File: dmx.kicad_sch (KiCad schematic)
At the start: 41 parts, among them J101 SJ2-25504B-SMT-TR, J102 CORTEX-DEBUG, J103 JAE_DX07S016JA1R1500, SW101 SW_Push, SW102 SW_Push, U101 LTC2851xDD, U102 ATSAMD51G, U103 AP2112K-3.3, Y101 32.768kHz

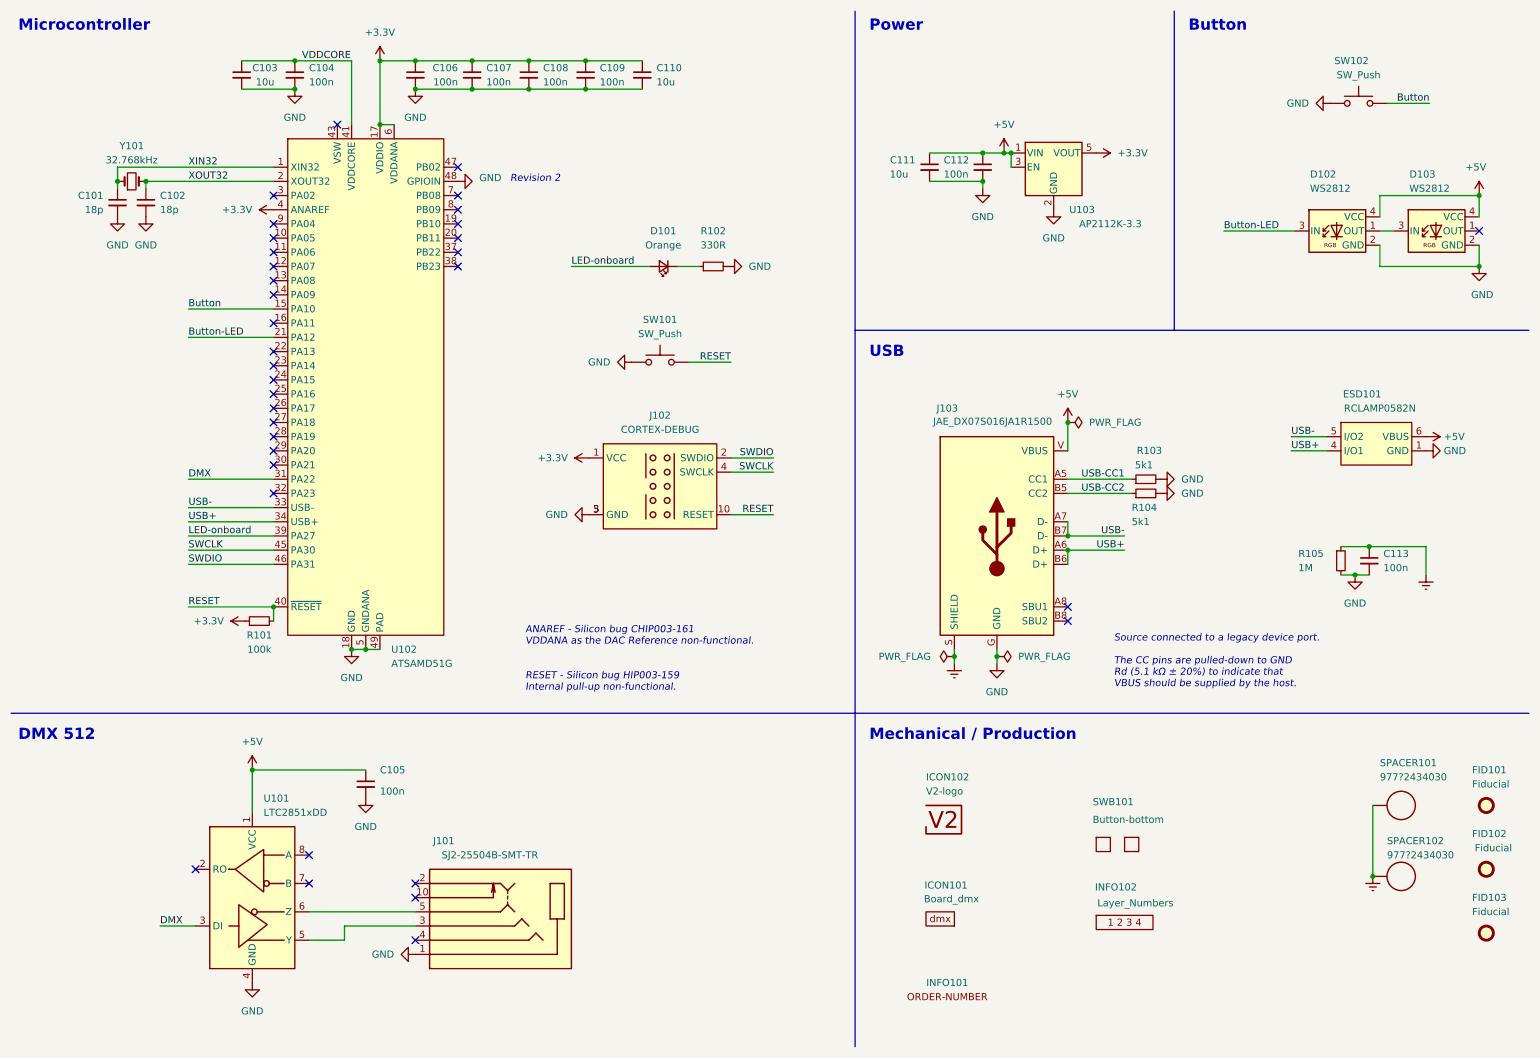
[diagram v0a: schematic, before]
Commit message: Update to KiCad 7.0
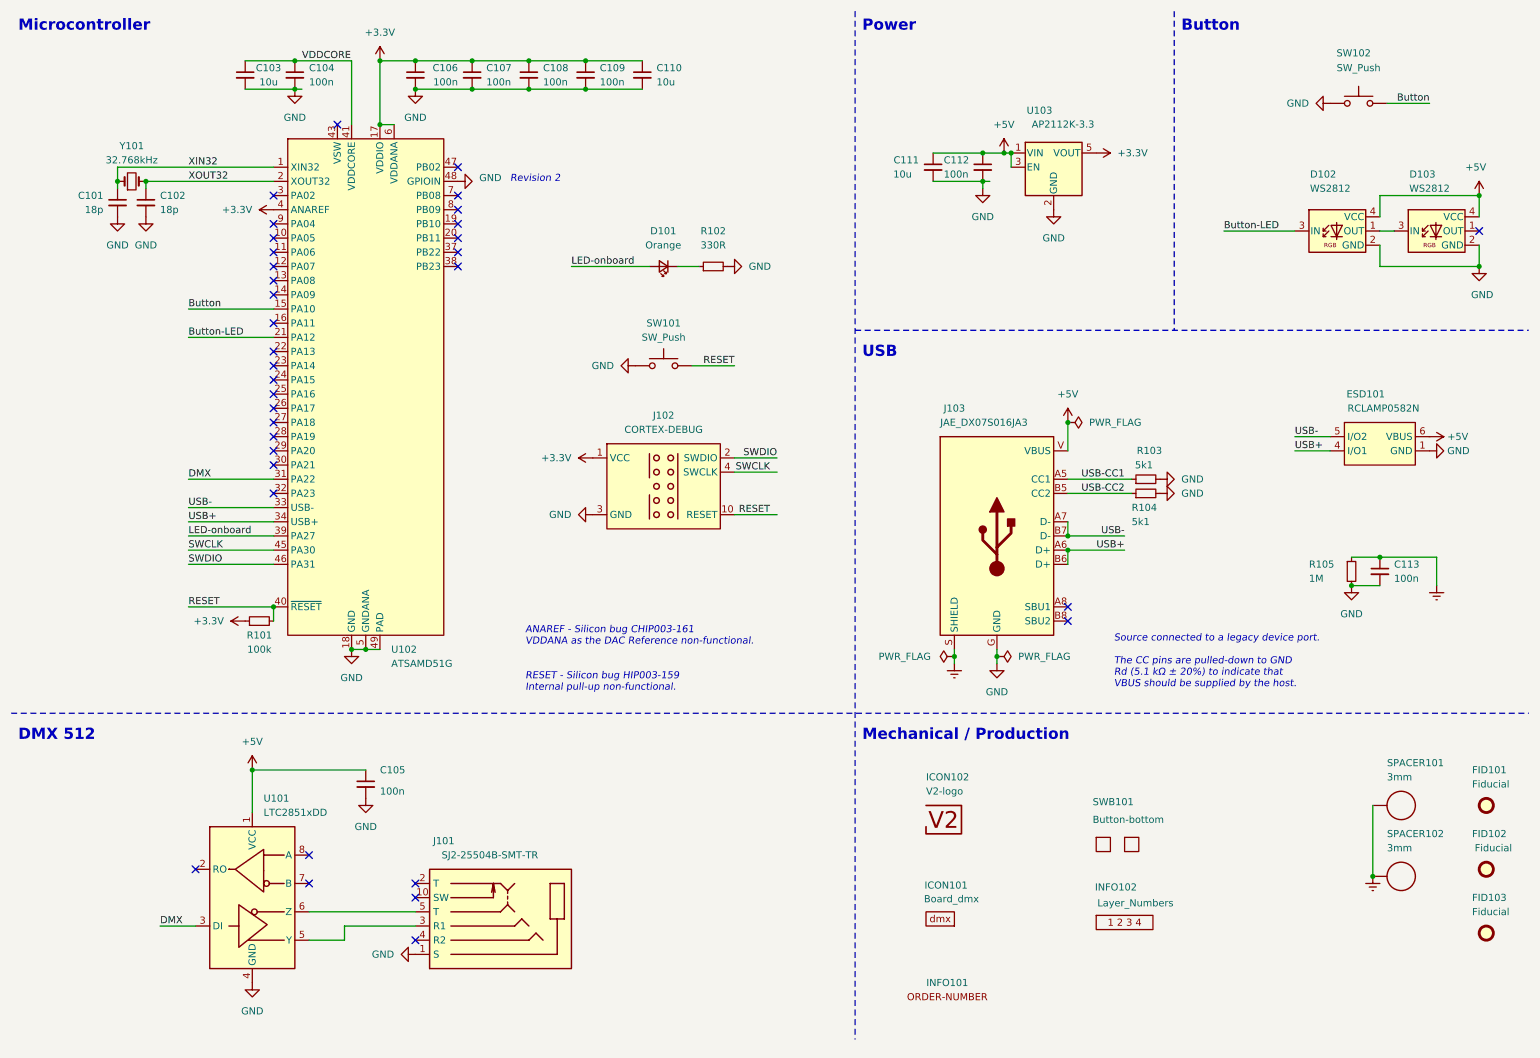
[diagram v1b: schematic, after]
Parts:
- J103: value JAE_DX07S016JA1R1500 -> JAE_DX07S016JA3; footprint V2_Connector_USB:JAE_DX07S016JA1R1500 -> V2_Connector_USB:JAE_DX07S016JA3; symbol V2_Connector_USB:JAE_DX07S016JA1R1500 -> V2_Connector_USB:JAE_DX07S016JA3
- SPACER101, SPACER102: value 977?2434030 -> 3mm; symbol V2_Spacer_Wurth:977?2434030 -> V2_Spacer_Wurth:9774030243
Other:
- moved on the sheet: C103, C111, C113, ESD101, R105, SW101
